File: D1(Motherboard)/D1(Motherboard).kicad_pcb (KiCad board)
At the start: 4 copper layers, 38 x 35 mm, 73 parts, among them J1 WR-FPC_0.5mm_ZIF_V, J2 USB_C_Receptacle_USB2.0, J3 B2B-PH-K-S, Q1 NX2301P.215, SW1 CHS-02A, U1 CP2102N-A01-GQFN28, U2 ICM-20602, U3 WR-FPC_0.5mm_ZIF_H, U4 MIC5353-3.3YMT, U5 FAN5331SX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

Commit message: Test Commit for CADLAB
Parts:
- moved J2 15.1 mm to (40.3, 35.0)
- moved J3 3.59 mm to (51.3, 35.3)
- moved C12 1.19 mm to (49.5, 40.3)
- moved C18 1.19 mm to (48.0, 40.3)
- moved D3 1.19 mm to (42.4, 42.6)
- moved Q1 1.19 mm to (39.8, 40.8)
- moved R2 1.19 mm to (44.9, 43.0)
- moved R3 1.19 mm to (42.4, 39.2)
- moved R9 1.19 mm to (34.9, 39.0)
- moved U6 1.19 mm to (45.2, 40.4)
- moved C20 1.19 mm to (39.9, 38.1)
- moved D5 1.19 mm to (36.9, 39.7)
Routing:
- net TXD0: track 16.5 -> 0.00 mm
- net RXD0: track 9.50 -> 0.00 mm
- net +BATT: track 48.4 -> 45.6 mm
- net CLK: track 51.8 -> 49.0 mm
- net GND: track 19.6 -> 17.1 mm, vias 36 -> 18
- net VBUS: track 7.27 -> 6.61 mm
- net Display2_CS: track 17.0 -> 17.6 mm

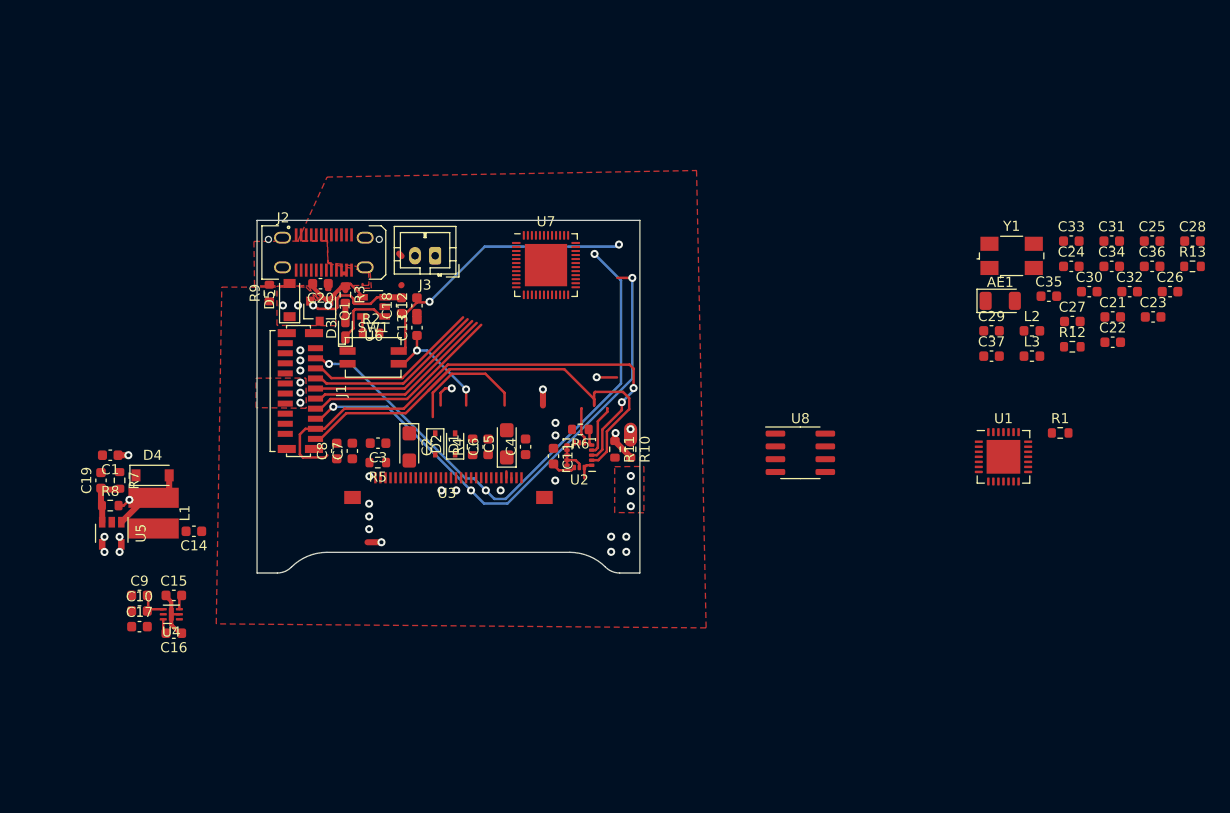
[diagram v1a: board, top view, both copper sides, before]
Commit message: Changed to KiCAD 6
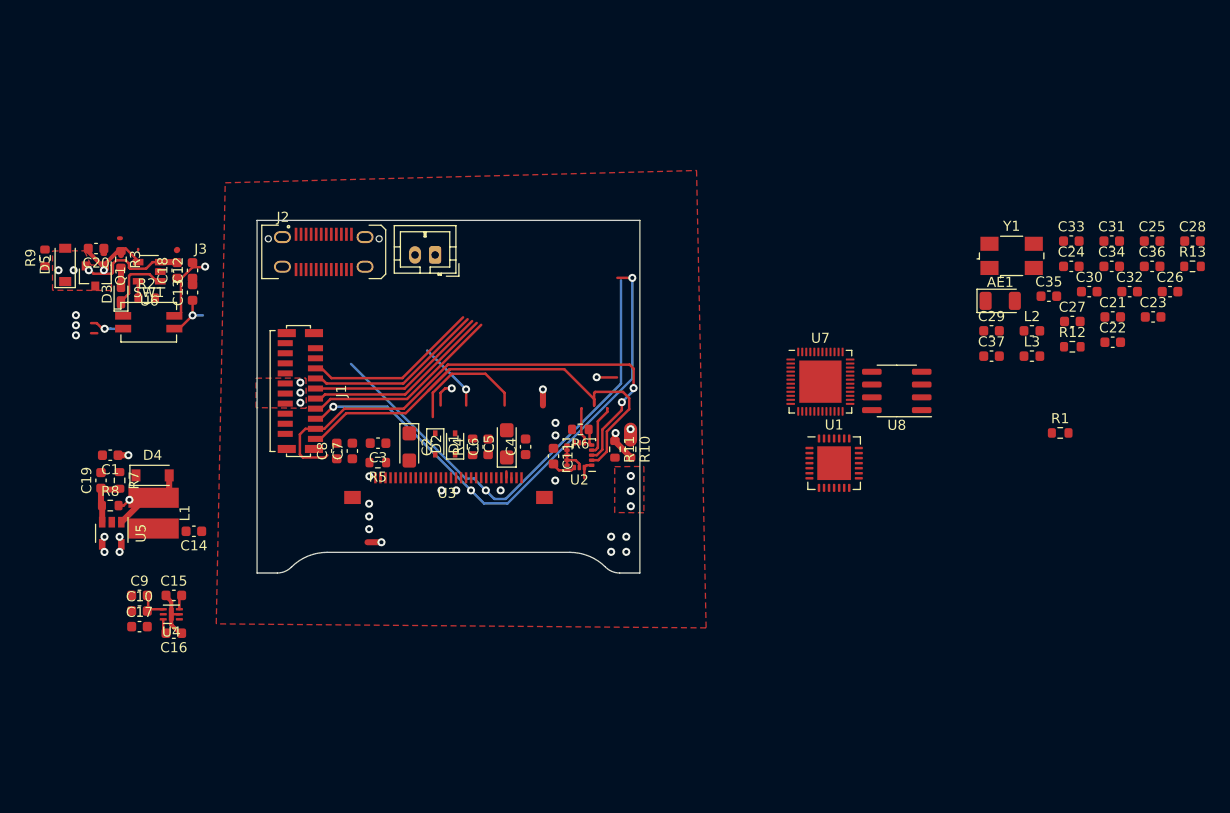
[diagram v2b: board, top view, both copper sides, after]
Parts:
- moved U7 29.6 mm to (89.5, 47.8)
- moved C20 22.5 mm to (17.6, 34.6)
- moved D3 22.5 mm to (20.1, 39.2)
- moved R3 22.5 mm to (20.1, 35.7)
- moved R9 22.5 mm to (12.6, 35.6)
- moved C12 22.5 mm to (27.2, 36.8)
- moved C13 22.5 mm to (27.2, 39.0)
- moved C18 22.5 mm to (25.7, 36.8)
- moved D5 22.5 mm to (14.6, 36.3)
- moved Q1 22.5 mm to (17.6, 37.4)
- moved R2 22.5 mm to (22.7, 39.6)
- moved SW1 22.5 mm to (22.9, 41.9)
- moved U6 22.5 mm to (22.9, 36.9)
- moved U1 16.8 mm to (90.9, 55.9)
- moved U8 11.4 mm to (97.1, 48.8), turned to 180 degrees
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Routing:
- net +BATT: track 45.6 -> 12.4 mm
- net Boot: track 28.2 -> 7.04 mm, vias 2 -> 1
- net RST: track 54.8 -> 51.1 mm, vias 3 -> 2
- removed copper zone on In1.Cu, net +5V
- removed copper zone on F.Cu, net VDD

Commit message: Upload New Version from USB
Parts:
- added D6: ESD5B5.0S, Diode_SMD:D_SOD-523, F.Cu at (89.6, 54.3)
- added D7: ESD5B5.0S, Diode_SMD:D_SOD-523, F.Cu at (88.1, 54.3)
- added D8: ESD5B5.0S, Diode_SMD:D_SOD-523, F.Cu at (86.6, 54.3)
- added Q2: MBT3904DW1, Package_TO_SOT_SMD:SOT-363_SC-70-6, F.Cu at (83.0, 44.3)
- added R14: 10k, Resistor_SMD:R_0603_1608Metric, F.Cu at (80.8, 44.4)
- added R15: 10k, Resistor_SMD:R_0603_1608Metric, F.Cu at (85.2, 44.4)
- added R16: 22.1k, Resistor_SMD:R_0603_1608Metric, F.Cu at (92.6, 51.4)
- added R17: 47.5k, Resistor_SMD:R_0603_1608Metric, F.Cu at (94.2, 51.4)
- added R18: 1k, Resistor_SMD:R_0603_1608Metric, F.Cu at (91.1, 51.4)
- moved R1 32.1 mm to (83.5, 41.1), turned to -90 degrees
- moved C27 29.5 mm to (85.1, 41.1), turned to -90 degrees
- moved R12 28.0 mm to (88.0, 35.3), turned to 90 degrees
- moved C35 23.9 mm to (89.0, 45.1), turned to 180 degrees
- moved C29 18.6 mm to (89.5, 35.3), turned to -90 degrees
- moved C20 18.3 mm to (35.4, 38.8), turned to 0 degrees
- moved C23 14.8 mm to (108.2, 45.0), turned to 180 degrees
- moved Y1 14.7 mm to (93.8, 34.6), turned to 180 degrees
- moved C37 14.5 mm to (92.0, 45.1), turned to 180 degrees
- moved L3 13.3 mm to (123.8, 46.9)
- moved C36 12.2 mm to (123.8, 48.5)
- moved C22 10.3 mm to (108.2, 43.4), turned to 180 degrees
- moved C30 9.01 mm to (123.8, 43.8)
- moved U8 8.05 mm to (96.5, 40.7), turned to 90 degrees
- moved C32 7.38 mm to (123.8, 45.4)
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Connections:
- J2 pad A6: TXD0 -> D+
- J2 pad A7: RXD0 -> D-
- J2 pad B6: TXD0 -> D+
- J2 pad B7: RXD0 -> D-
- U1 pad 24: unconnected-(U1-Pad24) -> RTS
- U1 pad 25: unconnected-(U1-Pad25) -> RX
- U1 pad 26: unconnected-(U1-Pad26) -> TX
- U1 pad 28: unconnected-(U1-Pad28) -> DTR
- U1 pad 29: Net-(U1-Pad29) -> GND
- U1 pad 3: Net-(U1-Pad29) -> GND
- U1 pad 4: unconnected-(U1-Pad4) -> D+
- U1 pad 5: unconnected-(U1-Pad5) -> D-
- U1 pad 6: unconnected-(U1-Pad6) -> VBUS
- U1 pad 7: unconnected-(U1-Pad7) -> VBUS
- U1 pad 8: unconnected-(U1-Pad8) -> Net-(U1-Pad8)
- U1 pad 9: unconnected-(U1-Pad9) -> Net-(U1-Pad9)
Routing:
- net DC: track 52.6 -> 0.00 mm, vias 3 -> 0
- net RST: track 51.1 -> 0.00 mm, vias 2 -> 0
- net CLK: track 49.0 -> 0.00 mm
- net Display6_CS: track 19.9 -> 0.00 mm
- net Display5_CS: track 19.2 -> 0.00 mm
- net Display4_CS: track 18.3 -> 0.00 mm
- net Display3_CS: track 17.9 -> 0.00 mm
- net Display2_CS: track 17.6 -> 0.00 mm
- net /ESP32-D0WDQ6-V3/SHD/SD2: track 0.00 -> 17.3 mm
- net Display1_CS: track 12.3 -> 0.00 mm
- net /ESP32-D0WDQ6-V3/IO33: track 13.8 -> 2.19 mm, vias 2 -> 0
- net Net-(C25-Pad2): track 0.00 -> 9.11 mm
- net /ESP32-D0WDQ6-V3/SDI/SD1: track 0.00 -> 8.89 mm
- net /ESP32-D0WDQ6-V3/SWP/SD3: track 0.00 -> 8.46 mm
- net Boot: track 7.04 -> 0.00 mm, vias 1 -> 0
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
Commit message: Cleaned a bit more
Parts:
- D3: footprint LED_SMD:LED_0603_1608Metric_Castellated -> LED_SMD:LED_0603_1608Metric
- J2: footprint Connector_USB:USB_C_Receptacle_JAE_DX07S024WJ3R400 -> D1(Motherboard):GCT_USB4120-03-C
- moved C12 99.4 mm to (123.3, 62.1)
- moved C13 99.4 mm to (123.3, 64.3)
- moved C18 99.4 mm to (121.8, 62.1)
- moved D5 99.4 mm to (110.7, 61.6)
- moved Q1 99.4 mm to (113.7, 62.7)
- moved R3 99.4 mm to (116.2, 61.0)
- moved SW1 99.4 mm to (119.0, 67.3)
- moved D3 99.4 mm to (116.2, 64.5)
- moved R2 99.4 mm to (118.8, 64.9)
- moved R9 99.4 mm to (108.7, 60.9)
- moved U6 99.4 mm to (119.0, 62.3)
- moved C17 92.0 mm to (113.4, 82.1), turned to 90 degrees
- moved C10 90.7 mm to (111.9, 82.1), turned to 90 degrees
- moved C9 89.4 mm to (110.3, 82.1), turned to 90 degrees
- moved C16 88.9 mm to (114.1, 79.1), turned to -90 degrees
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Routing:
- net GND: track 22.6 -> 15.3 mm
- net VBUS: track 12.7 -> 5.74 mm
- net Reset: track 9.93 -> 15.5 mm
- net D-: track 5.68 -> 1.49 mm, vias 2 -> 0
- net Net-(C26-Pad2): track 0.00 -> 3.97 mm
- net D+: track 5.23 -> 1.53 mm
- net +5V: track 1.50 -> 3.90 mm
- net Net-(C26-Pad1): track 0.00 -> 2.28 mm
- net +3V3: track 7.04 -> 8.74 mm
- removed copper zone on F.Cu, net +3V3
- removed copper zone on In1.Cu, net +3V3
- removed copper zone on F.Cu, net +5V

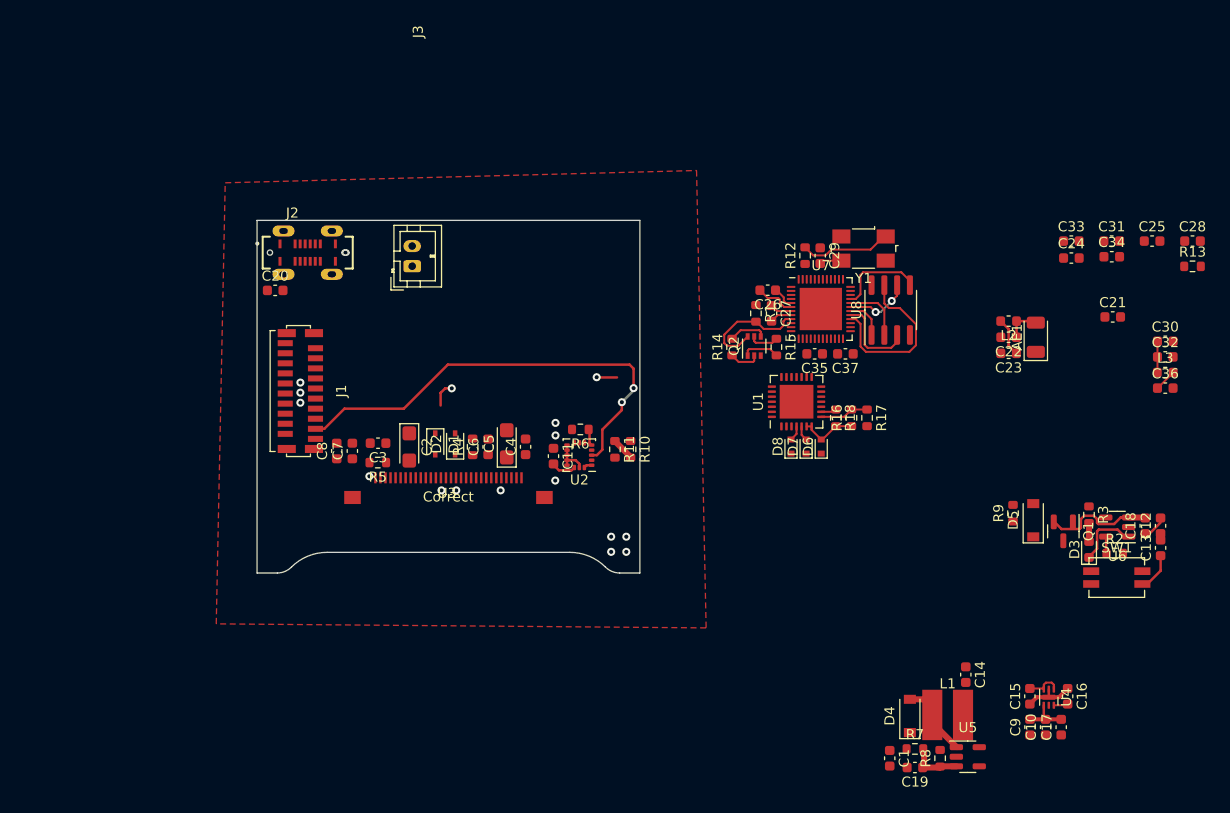
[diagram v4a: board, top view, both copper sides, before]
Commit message: Added ESP32 Datasheets to recources, started cleaning up layout for esp32
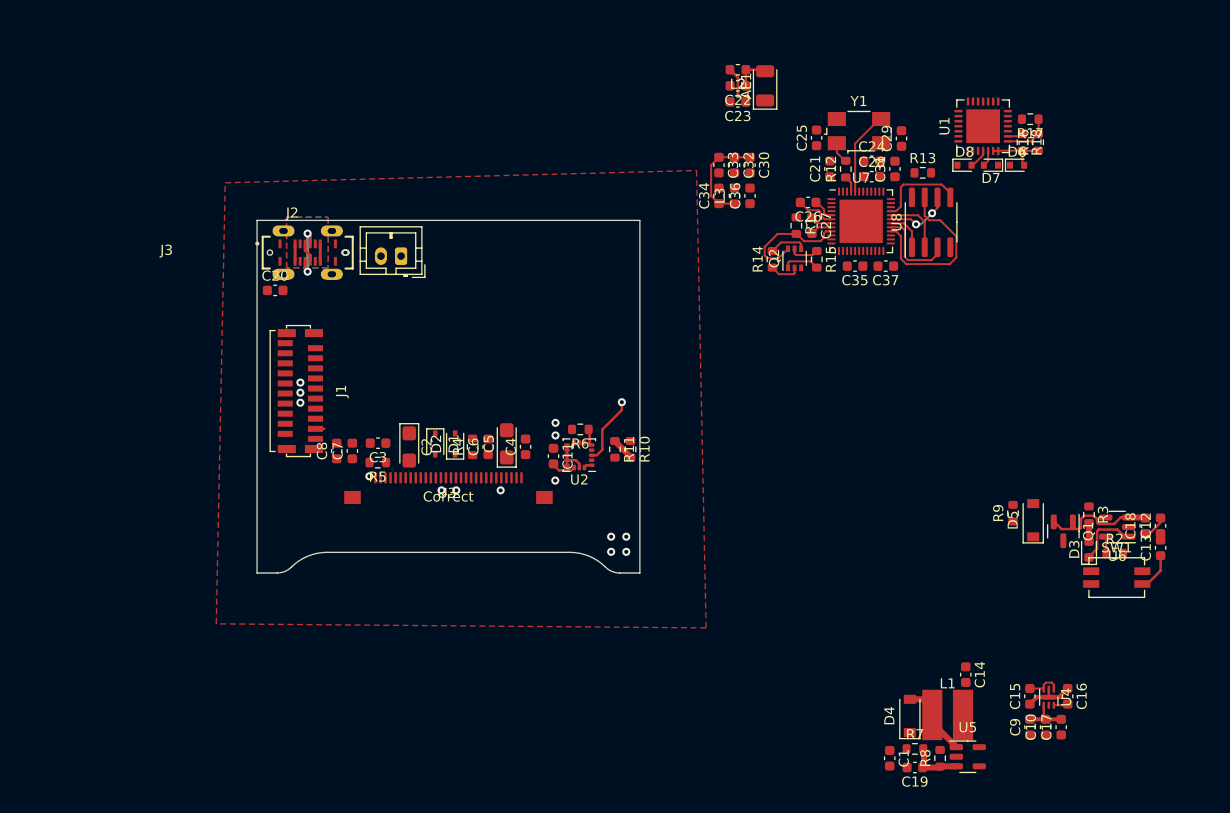
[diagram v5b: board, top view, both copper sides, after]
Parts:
- U7: footprint Package_DFN_QFN:QFN-48-1EP_6x6mm_P0.4mm_EP4.2x4.2mm -> Package_DFN_QFN:QFN-48-1EP_6x6mm_P0.4mm_EP4.3x4.3mm
- moved C32 46.8 mm to (81.0, 26.3), turned to -90 degrees
- moved L3 46.2 mm to (81.0, 29.4), turned to 90 degrees
- moved C36 45.4 mm to (82.6, 29.4), turned to 90 degrees
- moved C30 44.8 mm to (82.6, 26.3), turned to -90 degrees
- moved C34 39.5 mm to (79.5, 29.4), turned to 90 degrees
- moved AE1 36.7 mm to (84.1, 18.5)
- moved C22 36.7 mm to (81.4, 18.5)
- moved C23 36.7 mm to (81.4, 20.1)
- moved L2 36.7 mm to (81.4, 16.9)
- moved C33 35.8 mm to (79.5, 26.3), turned to -90 degrees
- moved C25 34.8 mm to (89.2, 23.6), turned to 90 degrees
- moved D6 34.0 mm to (109.1, 26.4), turned to 0 degrees
- moved R17 33.8 mm to (110.4, 21.8), turned to 180 degrees
- moved D7 33.4 mm to (106.5, 26.4), turned to 180 degrees
- moved R16 33.0 mm to (111.2, 24.1)
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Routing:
- net MOSI: track 45.0 -> 7.67 mm, vias 2 -> 1
- net Net-(C25-Pad2): track 9.11 -> 2.16 mm
- net +3V3: track 8.74 -> 15.5 mm
- net D-: track 1.49 -> 7.64 mm, vias 0 -> 2
- net XTAL_N: track 2.21 -> 8.36 mm
- net GND: track 15.3 -> 10.8 mm, vias 13 -> 11
- net VBUS: track 5.74 -> 9.79 mm
- net D+: track 1.53 -> 3.92 mm
- net VDD3P3: track 2.20 -> 0.01 mm
- net XTAL_P: track 0.00 -> 1.63 mm
- added copper zone on B.Cu, net VBUS
- added copper zone on F.Cu, net VBUS

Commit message: Changed VDD to VBUS to match other references
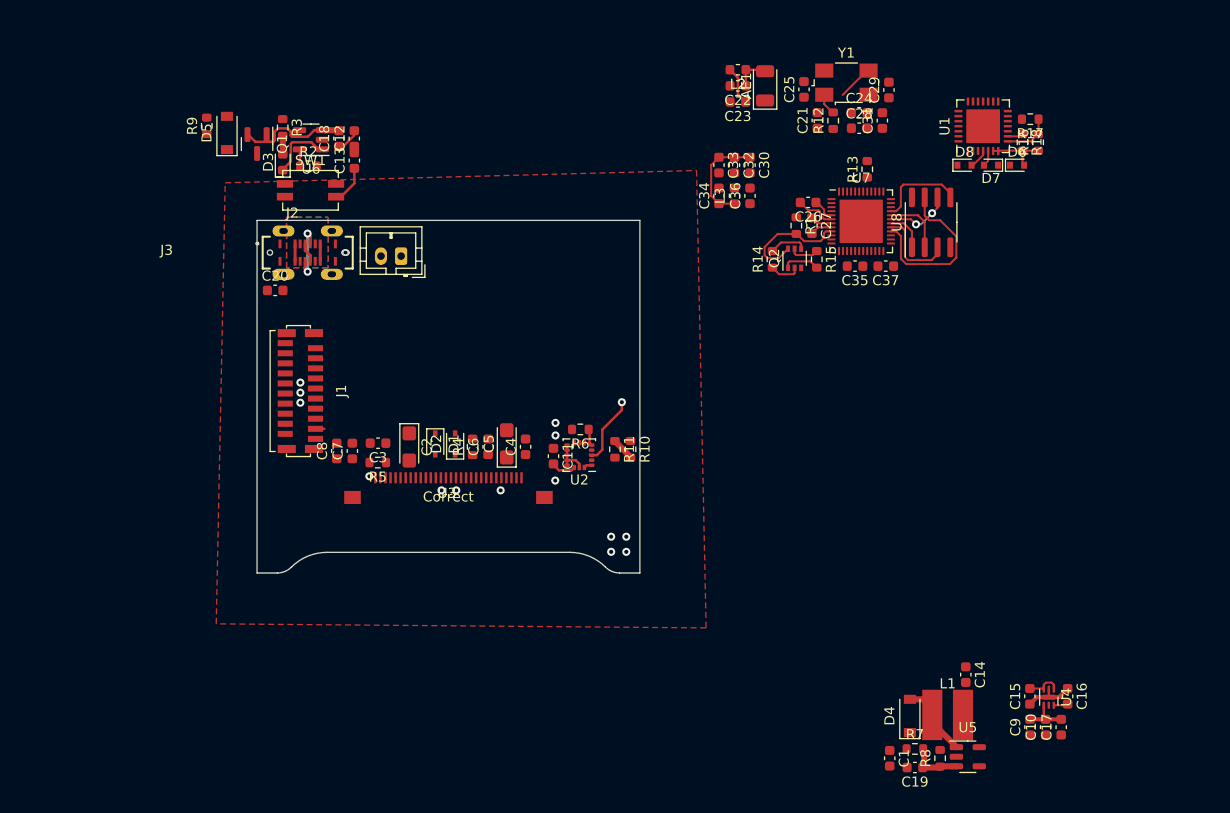
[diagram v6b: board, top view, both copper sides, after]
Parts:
- moved C12 88.8 mm to (43.3, 23.7)
- moved C13 88.8 mm to (43.3, 25.9)
- moved C18 88.8 mm to (41.8, 23.7)
- moved D3 88.8 mm to (36.2, 26.1)
- moved D5 88.8 mm to (30.6, 23.2)
- moved Q1 88.8 mm to (33.6, 24.3)
- moved R2 88.8 mm to (38.7, 26.5)
- moved R3 88.8 mm to (36.2, 22.6)
- moved R9 88.8 mm to (28.6, 22.5)
- moved SW1 88.8 mm to (38.9, 28.8)
- moved U6 88.8 mm to (39.0, 23.8)
- moved R13 5.52 mm to (94.2, 26.8), turned to 90 degrees
- moved C21 4.97 mm to (89.2, 21.9)
- moved C28 4.97 mm to (93.4, 22.7)
- moved R12 4.97 mm to (90.8, 21.9)
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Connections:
- D5 pad 2: VDD -> VBUS
- Q1 pad 1: VDD -> VBUS
- R9 pad 2: VDD -> VBUS
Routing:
- net XTAL_N: track 8.36 -> 3.58 mm
- net XTAL_P: track 1.63 -> 0.00 mm
